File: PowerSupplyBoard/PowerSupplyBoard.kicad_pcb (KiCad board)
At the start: 4 copper layers, 50 x 75 mm, 93 parts, among them J101 BATTERY, J102 I2C, J103 USB_C, J104 PWR, J105 DATA1, Q101 BSH205G2A, Q102 DMP6050SSD, Q103 2N7002H, SW101 SW_SPDT, U101 TPS63021, U102 MCP73834T, U103 MAX17578ATC, U104 CYPD3177-24LQ, U105 CS5173

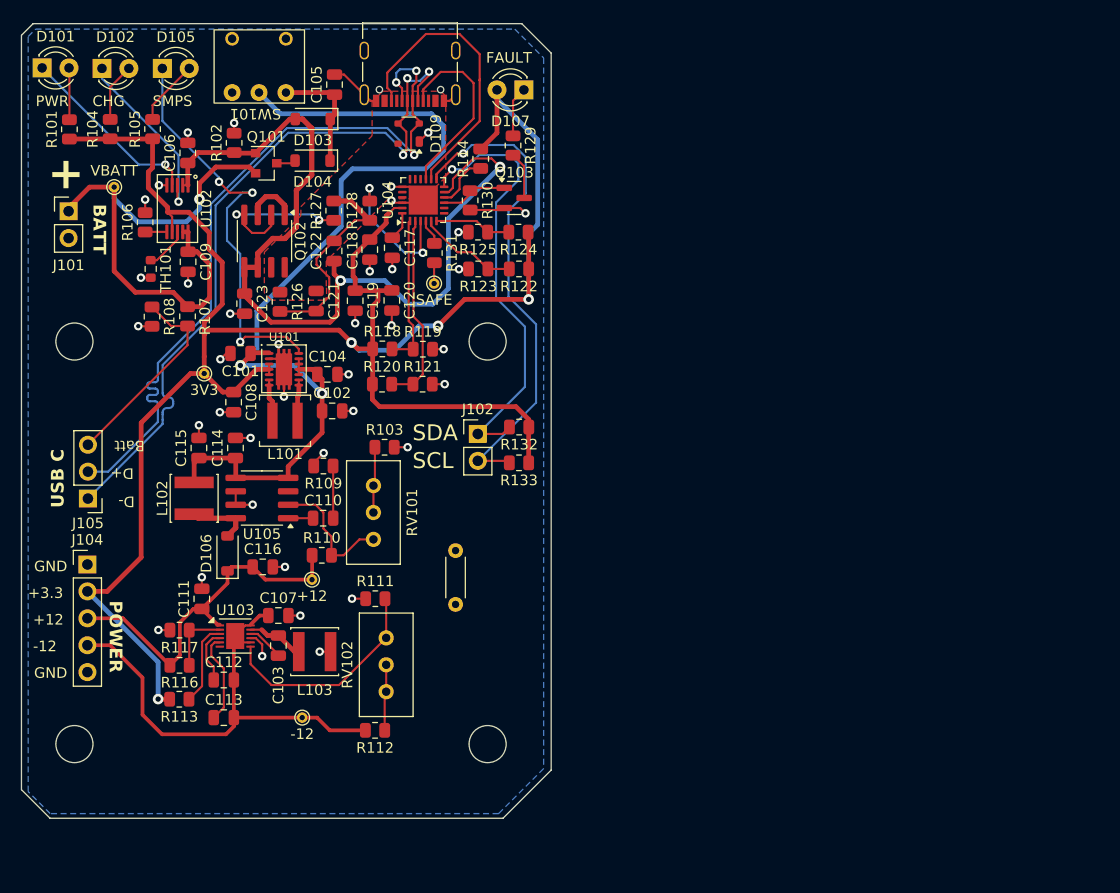
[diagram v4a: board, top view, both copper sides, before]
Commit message: psu schematic updates
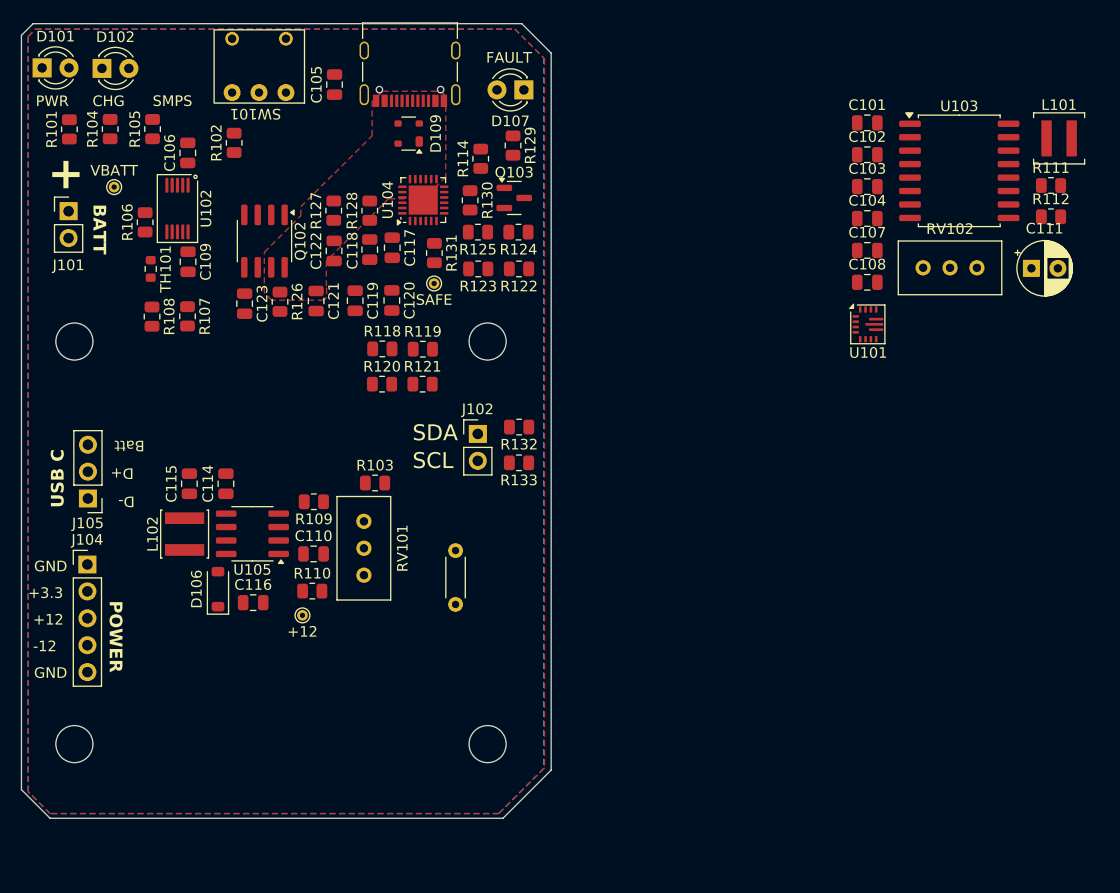
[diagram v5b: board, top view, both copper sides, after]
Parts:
- removed C112: 4n7, Capacitor_SMD:C_0805_2012Metric
- removed C113: 2u2, Capacitor_SMD:C_0805_2012Metric
- removed D103, D104: PMEG3030, Diode_SMD:D_SOD-123
- removed D105: SMPS, LED_THT:LED_D3.0mm
- removed L103: 22uH, Inductor_SMD:L_Changjiang_FNR4010S
- removed Q101: BSH205G2A, PCM_4ms_Package_SOT:SOT-23
- removed R113: 4k7, Resistor_SMD:R_0805_2012Metric
- removed R116: 330k, Resistor_SMD:R_0805_2012Metric
- removed R117: 100k, Resistor_SMD:R_0805_2012Metric
- removed TP101: -12, TestPoint:TestPoint_THTPad_D1.0mm_Drill0.5mm_VAL
- removed TP102: 3V3, TestPoint:TestPoint_THTPad_D1.0mm_Drill0.5mm_VAL
- C103: value 100n -> 10u
- C105: value 1u -> 10u
- C111: value 4u7 -> 330u; footprint Capacitor_SMD:C_0805_2012Metric -> Capacitor_THT:CP_Radial_D5.0mm_P2.50mm
- R105: value 680 -> 47k
- R111: value 470k -> 5k1
- R112: value 33k -> 100k
- U101: value TPS63021 -> TPS63070; footprint Package_SON:Texas_S-PVSON-N14 -> Package_DFN_QFN:TXN_QFN15
- U103: value MAX17578ATC -> NCV33163; footprint Package_DFN_QFN:TDFN-12-1EP_3x3mm_P0.4mm_EP1.7x2.45mm -> Package_SO:SOIC-16W_7.5x10.3mm_P1.27mm
- moved C111 84.3 mm to (95.3, 23.1), turned to 0 degrees
- moved U103 81.2 mm to (88.5, 13.9)
- moved R112 80.1 mm to (97.2, 18.2), turned to 0 degrees
- moved L101 77.8 mm to (97.9, 10.8), turned to 0 degrees
- moved R111 74.8 mm to (97.2, 15.3)
- moved C103 70.5 mm to (79.8, 15.4), turned to 0 degrees
- moved RV102 65.8 mm to (90.2, 23.0), turned to 0 degrees
- moved C107 65.4 mm to (79.8, 21.4), turned to 0 degrees
- moved C101 63.0 mm to (79.8, 9.36), turned to 0 degrees
- moved C108 60.9 mm to (79.8, 24.4), turned to 0 degrees
- moved C102 56.0 mm to (79.8, 12.4)
- moved U101 55.2 mm to (79.9, 28.4)
- moved C104 53.0 mm to (79.8, 18.4)
- moved C116 3.49 mm to (21.9, 54.6)
- moved D106 3.49 mm to (18.6, 53.4)
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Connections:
- C103 pad 1: Net-(U103-BST) -> V_PWR
- C103 pad 2: Net-(U103-LX) -> GND
- C104 pad 1: V_PWR -> Net-(U101-VAUX)
- C105 pad 1: VCC -> +3.3V
- C107 pad 1: GND -> +3.3V
- C107 pad 2: -12V -> GND
- C111 pad 1: +12V -> +3.3V
- L101 pad 1: Net-(L101-Pad1) -> Net-(U101-L1)
- L101 pad 2: Net-(L101-Pad2) -> Net-(U101-L2)
- R102 pad 1: VDD -> V_PWR
- R102 pad 2: GND -> Net-(U101-EN)
- R105 pad 2: Net-(D105-A) -> Net-(U101-FB)
- R111 pad 1: GND -> Net-(R111-Pad1)
- R111 pad 2: Net-(U103-FB) -> GND
- R112 pad 1: Net-(R112-Pad1) -> +3.3V
- R112 pad 2: -12V -> Net-(U101-PG)
- RV102 pad 1: Net-(U103-FB) -> Net-(U101-FB)
- RV102 pad 2: Net-(R112-Pad1) -> Net-(R111-Pad1)
- RV102 pad 3: Net-(R112-Pad1) -> Net-(R111-Pad1)
- SW101 pad 3: unconnected-(SW101-C-Pad3) -> GND
- U101 pad 1: V_PWR -> Net-(U101-EN)
- U101 pad 10: V_PWR -> GND
- U101 pad 11: V_PWR -> Net-(U101-L1)
- U101 pad 14: Net-(D105-K) -> Net-(U101-EN)
- U101 pad 2: GND -> Net-(U101-PG)
- U101 pad 3: +3.3V -> Net-(U101-VAUX)
- U101 pad 4: +3.3V -> GND
- U101 pad 5: +3.3V -> Net-(U101-FB)
- U101 pad 6: Net-(L101-Pad2) -> GND
- U101 pad 7: Net-(L101-Pad2) -> +3.3V
- U101 pad 8: Net-(L101-Pad1) -> +3.3V
- U101 pad 9: Net-(L101-Pad1) -> Net-(U101-L2)
- U103 pad 1: +12V -> unconnected-(U103-LVO-Pad1)
- U103 pad 10: Net-(U103-BST) -> Net-(U103-SWC-Pad10)
- U103 pad 11: Net-(U103-LX) -> Net-(U103-SWC-Pad10)
- U103 pad 12: -12V -> Net-(U103-GND-Pad12)
- U103 pad 13: -12V -> Net-(U103-GND-Pad12)
- U103 pad 2: Net-(U103-EN/UVLO) -> unconnected-(U103-FB2-Pad2)
- U103 pad 3: /NRST -> unconnected-(U103-FB1-Pad3)
- U103 pad 4: Net-(U103-SS) -> Net-(U103-GND-Pad12)
- U103 pad 5: Net-(U103-VCC) -> Net-(U103-GND-Pad12)
- U103 pad 7: Net-(U103-FB) -> unconnected-(U103-VCC-Pad7)
- U103 pad 8: -12V -> unconnected-(U103-ISense-Pad8)
- U103 pad 9: GND -> unconnected-(U103-DC-Pad9)
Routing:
- net +3.3V: track 200.7 -> 0.00 mm, vias 4 -> 0
- net V_PWR: track 92.9 -> 0.00 mm, vias 2 -> 0
- net VDD: track 84.9 -> 0.00 mm, vias 2 -> 0
- net USBC_D+: track 71.3 -> 0.00 mm, vias 3 -> 0
- net USBC_D-: track 69.3 -> 0.00 mm, vias 3 -> 0
- net GND: track 63.3 -> 0.00 mm, vias 38 -> 0
- net VBATT: track 51.2 -> 0.00 mm, vias 1 -> 0
- net -12V: track 46.8 -> 0.00 mm
- net SCL: track 46.3 -> 0.00 mm, vias 1 -> 0
- net SDA: track 41.7 -> 0.00 mm, vias 1 -> 0
- net Net-(D105-K): track 39.2 -> 0.00 mm, vias 3 -> 0
- net +12V: track 34.5 -> 0.00 mm
- net /CC2: track 27.6 -> 0.00 mm
- net Net-(U103-FB): track 20.9 -> 0.00 mm
- net Net-(C121-Pad2): track 20.1 -> 0.00 mm
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- added copper zone on F.Cu, net GND
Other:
- board text added: "Rev. 4 Aug. 2024 Hayden Setlik"
- board text removed: "Rev. 3 July 2024 Hayden Setlik"

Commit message: psu rev5 layout
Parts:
- added C112: 1n, Capacitor_SMD:C_0805_2012Metric, F.Cu at (14.2, 67.5)
- added C113: 330u, Capacitor_THT:CP_Radial_D5.0mm_P2.50mm, F.Cu at (20.1, 57.5)
- added C124: 1u, Capacitor_SMD:C_0805_2012Metric, F.Cu at (14.2, 71.0)
- added C125: 220u, Capacitor_THT:CP_Radial_D5.0mm_P2.50mm, F.Cu at (43.8, 51.9)
- added C126: 220u, Capacitor_THT:CP_Radial_D5.0mm_P2.50mm, F.Cu at (43.8, 60.2)
- added C127: 10u, Capacitor_SMD:C_0805_2012Metric, F.Cu at (11.0, 63.7)
- added C128: 1u, Capacitor_SMD:C_0805_2012Metric, F.Cu at (25.8, 13.8)
- added D103: PMEG3030, Diode_SMD:D_SOD-123, F.Cu at (44.8, 68.5)
- added D104: PMEG3030, Diode_SMD:D_SOD-123, F.Cu at (28.7, 9.15)
- added D105: PMEG3030, Diode_SMD:D_SOD-123, F.Cu at (29.3, 13.1)
- added D108: SMPS, LED_THT:LED_D3.0mm, F.Cu at (13.3, 4.22)
- added L103: 180u, Inductor_SMD:L_Coilcraft_MSS1278-XXX, F.Cu at (35.2, 63.8)
- added Q101: BSH205G2A, PCM_4ms_Package_SOT:SOT-23, F.Cu at (21.3, 14.6)
- added R113: 5k1, Resistor_SMD:R_0805_2012Metric, F.Cu at (13.3, 63.7)
- added R116: 0.075, Resistor_SMD:R_0805_2012Metric, F.Cu at (14.2, 75.6)
- added R117: 10k, Resistor_SMD:R_0805_2012Metric, F.Cu at (25.2, 9.72)
- added R135: 470, Resistor_SMD:R_0805_2012Metric, F.Cu at (11.3, 10.0)
- added RV103: 10k, Potentiometer_THT:Potentiometer_Bourns_3296W_Vertical, F.Cu at (37.3, 74.8)
- added TP101: 3V3, TestPoint:TestPoint_THTPad_D1.0mm_Drill0.5mm_VAL, F.Cu at (33.5, 39.0)
- added TP102: -12, TestPoint:TestPoint_THTPad_D1.0mm_Drill0.5mm_VAL, F.Cu at (9.82, 67.8)
- moved C111 89.7 mm to (11.6, 55.2)
- moved U103 85.7 mm to (22.4, 68.5)
- moved R111 82.0 mm to (16.6, 30.4)
- moved RV102 79.6 mm to (11.8, 36.6), turned to -90 degrees
- moved R112 79.3 mm to (20.8, 39.5), turned to 90 degrees
- moved L101 73.6 mm to (28.5, 35.3), turned to -90 degrees
- moved C107 62.3 mm to (21.5, 43.5), turned to -90 degrees
- moved C104 61.9 mm to (20.3, 35.4), turned to 180 degrees
- moved C103 58.0 mm to (24.1, 31.4), turned to 90 degrees
- moved C101 56.5 mm to (27.6, 30.7), turned to 90 degrees
- moved U101 56.2 mm to (24.1, 35.2)
- moved C108 53.1 mm to (29.2, 40.4), turned to -90 degrees
- moved C102 52.1 mm to (31.1, 30.8), turned to 90 degrees
- moved C105 34.8 mm to (25.8, 40.4), turned to -90 degrees
- moved R105 27.8 mm to (16.4, 37.5), turned to 180 degrees
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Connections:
- R101 pad 1: +3.3V -> VDD
- R104 pad 1: +3.3V -> VDD
- U102 pad 7: +3.3V -> VDD
- U103 pad 10: Net-(U103-SWC-Pad10) -> Net-(U103-DC)
- U103 pad 11: Net-(U103-SWC-Pad10) -> Net-(U103-DC)
- U103 pad 12: Net-(U103-GND-Pad12) -> -12V
- U103 pad 13: Net-(U103-GND-Pad12) -> -12V
- U103 pad 2: unconnected-(U103-FB2-Pad2) -> Net-(U103-FB2)
- U103 pad 4: Net-(U103-GND-Pad12) -> -12V
- U103 pad 5: Net-(U103-GND-Pad12) -> -12V
- U103 pad 6: unconnected-(U103-CAP-Pad6) -> Net-(U103-CAP)
- U103 pad 7: unconnected-(U103-VCC-Pad7) -> +12V
- U103 pad 8: unconnected-(U103-ISense-Pad8) -> Net-(U103-DC)
- U103 pad 9: unconnected-(U103-DC-Pad9) -> Net-(U103-DC)
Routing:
- net USBC_D+: track 0.00 -> 66.0 mm, vias 0 -> 2
- net USBC_D-: track 0.00 -> 65.4 mm, vias 0 -> 2
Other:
- board size 50 x 75 mm -> 50 x 80 mm

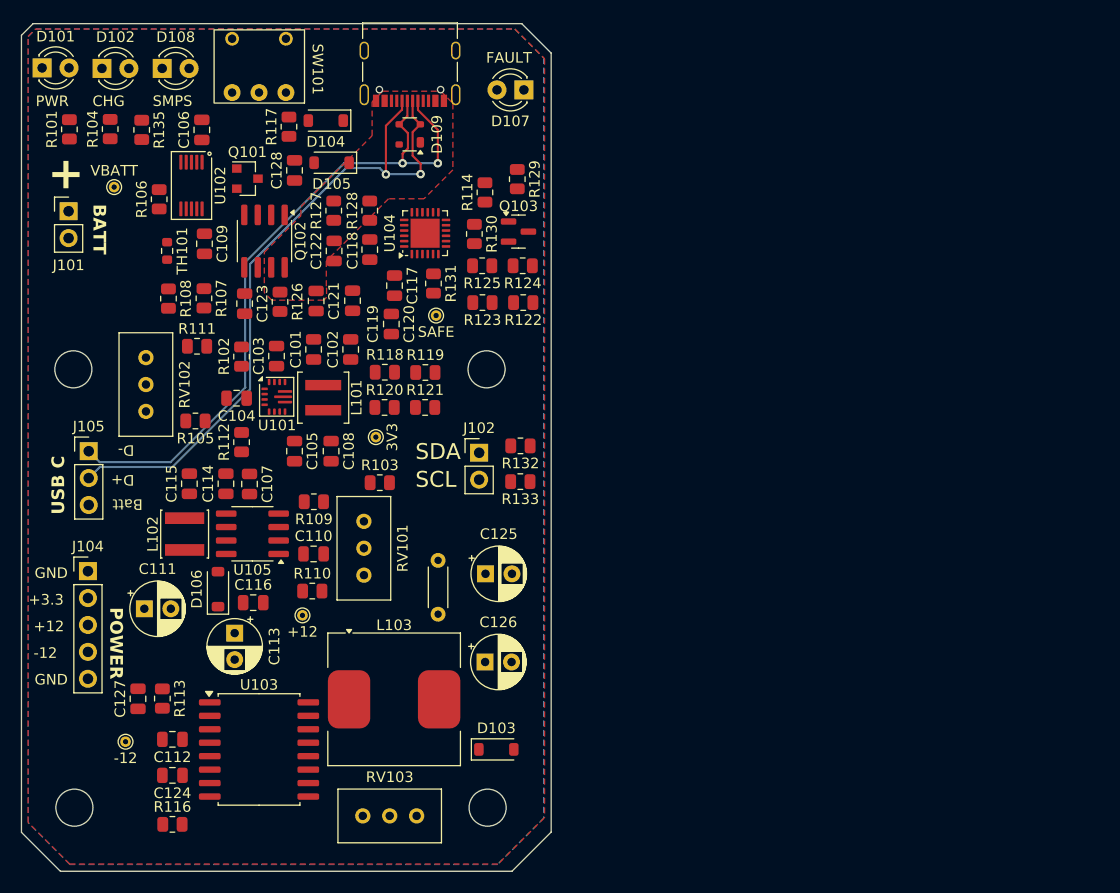
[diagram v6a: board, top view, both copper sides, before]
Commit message: psu rev5 routing
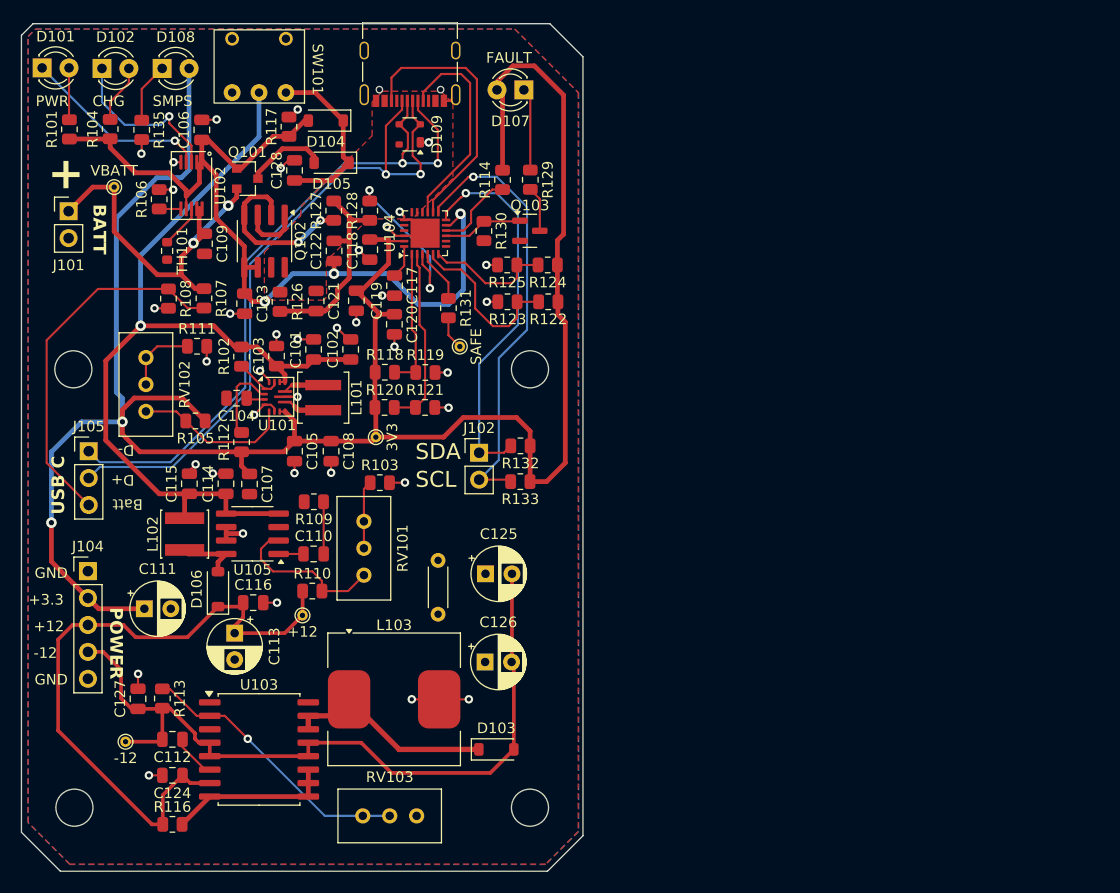
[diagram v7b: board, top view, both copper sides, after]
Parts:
- moved REF** 4.10 mm to (48.0, 32.6)
- moved REF** 4.00 mm to (48.0, 74.0)
- moved TP104 3.68 mm to (41.4, 30.5), turned to 90 degrees
- moved R131 2.72 mm to (40.3, 26.9)
- moved R122 2.36 mm to (49.7, 26.2)
- moved R123 2.36 mm to (45.9, 26.2)
- moved R124 2.36 mm to (49.7, 22.8)
- moved R125 2.36 mm to (45.8, 22.8)
- moved R114 2.04 mm to (45.4, 14.7)
- moved R129 1.23 mm to (48.0, 14.7)
- moved Q103 1.08 mm to (48.0, 19.6)
- moved R130 0.94 mm to (43.6, 19.6)
- moved C119 0.36 mm to (31.6, 26.1)
- moved C120 0.29 mm to (35.2, 28.4)
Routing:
- net +3.3V: track 0.00 -> 212.0 mm, vias 0 -> 2
- net V_PWR: track 0.00 -> 85.5 mm, vias 0 -> 1
- net VDD: track 0.00 -> 84.5 mm, vias 0 -> 3
- net -12V: track 0.00 -> 73.5 mm
- net +12V: track 0.00 -> 62.9 mm
- net GND: track 0.00 -> 58.9 mm, vias 0 -> 37
- net SCL: track 0.00 -> 41.9 mm, vias 0 -> 1
- net SDA: track 0.00 -> 36.4 mm, vias 0 -> 1
- net BATT_REF: track 0.00 -> 34.8 mm
- net VBATT: track 0.00 -> 34.7 mm, vias 0 -> 2
- net Net-(U103-FB2): track 0.00 -> 26.4 mm, vias 0 -> 1
- net /CC2: track 0.00 -> 25.3 mm
- net /CC1: track 0.00 -> 20.2 mm
- net Net-(D103-K): track 0.00 -> 20.0 mm
- net Net-(C121-Pad2): track 0.00 -> 19.8 mm
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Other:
- board size 50 x 80 mm -> 53 x 80 mm

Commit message: psu rev5 sent to fab
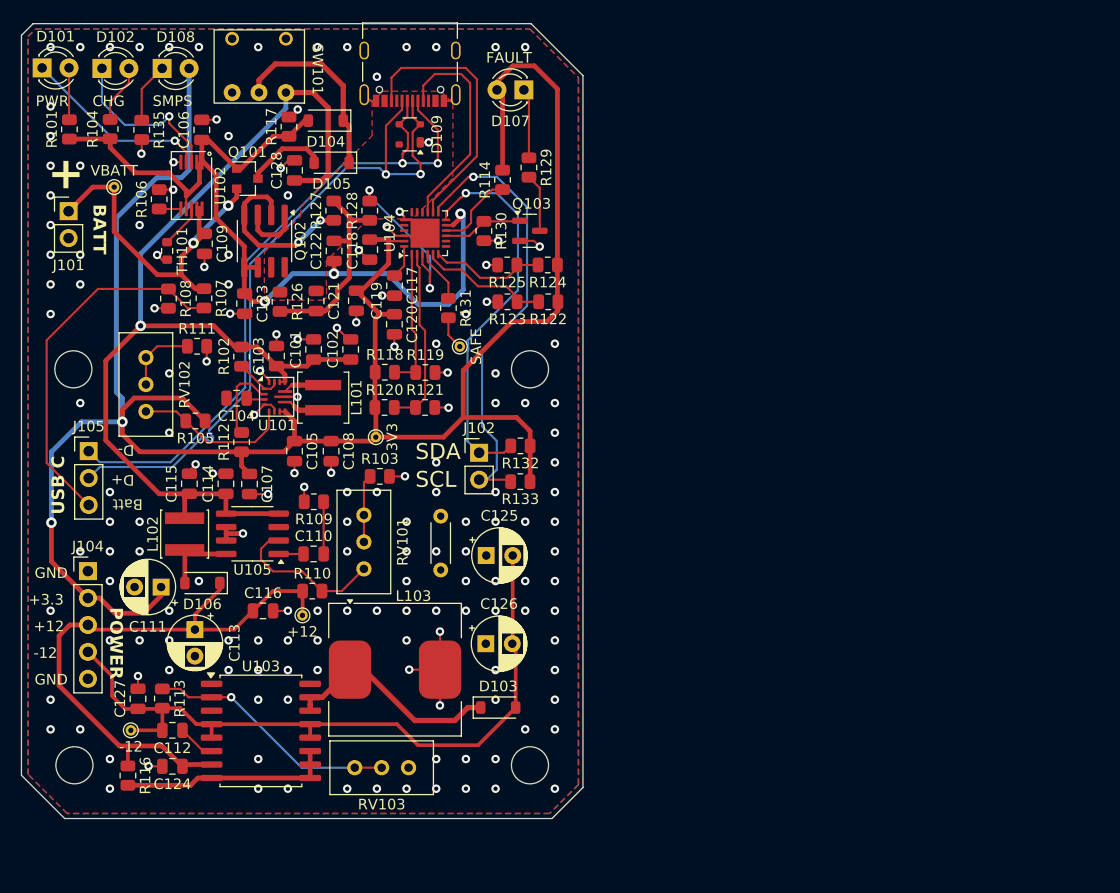
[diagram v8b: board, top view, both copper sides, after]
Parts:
- moved R116 6.23 mm to (10.1, 71.0), turned to -90 degrees
- moved RV103 4.61 mm to (36.5, 70.2)
- moved R115 4.18 mm to (39.6, 51.6)
- moved REF** 4.00 mm to (48.0, 70.0)
- moved REF** 4.00 mm to (5.00, 70.0)
- moved D103 3.95 mm to (45.0, 64.5)
- moved C113 3.76 mm to (16.4, 57.2)
- moved L103 2.80 mm to (35.3, 61.0)
- moved C111 2.59 mm to (13.2, 53.2), turned to 180 degrees
- moved U103 1.76 mm to (22.6, 66.8)
- moved C126 1.73 mm to (43.8, 58.5)
- moved C125 1.73 mm to (43.9, 50.2)
- moved D106 1.58 mm to (17.1, 52.8), turned to 180 degrees
- moved C116 1.21 mm to (22.8, 55.4)
- moved TP102 1.19 mm to (10.3, 66.7)
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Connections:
- C101 pad 1: V_PWR -> VCC
- C102 pad 1: V_PWR -> VCC
- C103 pad 1: V_PWR -> VCC
- C114 pad 1: V_PWR -> VCC
- C115 pad 1: V_PWR -> VCC
- D104 pad 1: VCC -> Net-(D104-K)
- D105 pad 1: VCC -> Net-(D104-K)
- L102 pad 2: V_PWR -> VCC
- R102 pad 1: V_PWR -> VCC
- SW101 pad 2: V_PWR -> Net-(D104-K)
- SW101 pad 3: GND -> unconnected-(SW101-C-Pad3)
- U101 pad 12: V_PWR -> VCC
- U101 pad 13: V_PWR -> VCC
- U105 pad 4: V_PWR -> VCC
- U105 pad 5: V_PWR -> VCC
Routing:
- net V_PWR: track 85.5 -> 0.00 mm, vias 1 -> 0
- net VCC: track 16.6 -> 100.9 mm, vias 0 -> 1
- net Net-(D104-K): track 0.00 -> 18.1 mm
- net GND: track 58.9 -> 73.7 mm, vias 37 -> 167
- net +12V: track 62.9 -> 57.0 mm
- net -12V: track 73.5 -> 68.7 mm
- net Net-(U103-DC): track 15.6 -> 20.0 mm
- net /I_COARSE: track 16.2 -> 12.3 mm
- net Net-(U103-FB2): track 26.4 -> 23.8 mm
- net SCL: track 41.9 -> 43.4 mm
- net USBC_D+: track 66.0 -> 67.3 mm
- net Net-(Q103-D): track 4.28 -> 5.49 mm
- net Net-(D106-A): track 6.07 -> 7.22 mm
- net SDA: track 36.4 -> 37.3 mm
- net Net-(D103-K): track 20.0 -> 20.9 mm
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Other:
- board size 53 x 80 mm -> 53 x 75 mm
- board text added: "Rev. 5 Aug. 2024 Hayden Setlik"
- board text removed: "Rev. 4 Aug. 2024 Hayden Setlik"
